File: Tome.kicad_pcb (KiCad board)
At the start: 2 copper layers, 13 x 1.4 mm, 155 parts, among them J201 USB_C_Receptacle_USB2.0_14P, J202 SD_Card_Receptacle, J203 [battery], J204 FFC Connector, J205 SM03B-SRSS-TB, J301 FFC Connector, J302 AudioJack3, J401 FPC Connector, J501 FPC Connector, J601 Conn_01x02_Pin, J602 Conn_01x02_Pin, J603 Conn_01x02_Pin, J604 Conn_01x02_Pin, J701 Conn_01x02_Pin, J702 Conn_01x02_Pin, J703 Conn_01x02_Pin, J704 Conn_01x02_Pin, Q201 DMG3415, Q202 DMG3415, Q401 Si1308EDL, Q501 Si1308EDL, SW201 [bootstrap button], SW202 [reset button], SW203 SW_SPST, SW301 SW_SPST, SW302 SW_SPST, SW601 RotaryEncoder_Switch, SW701 RotaryEncoder_Switch, U201 MCP73831-2-OT, U202 XC6220B331MR, U203 W25Q128JVS, U204 RP2350A, U205 74AHC1G04, U206 W25Q128JVS, U301 TLV70033_SOT23-5, U302 PCM5102A, U303 PAM8908, Y201 ABM8-272-T3

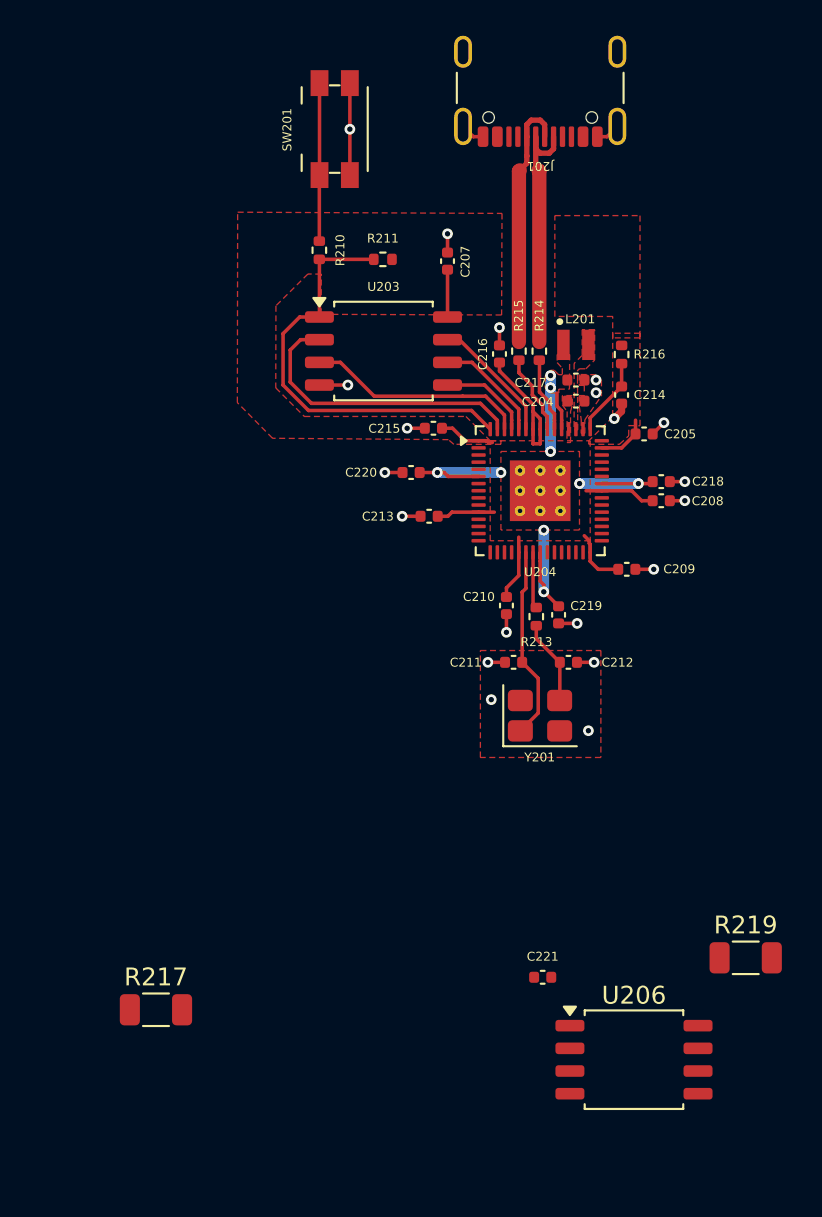
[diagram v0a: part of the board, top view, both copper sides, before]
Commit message: secondary flash
optional, don't anticipate needing it but who knows, could be useful
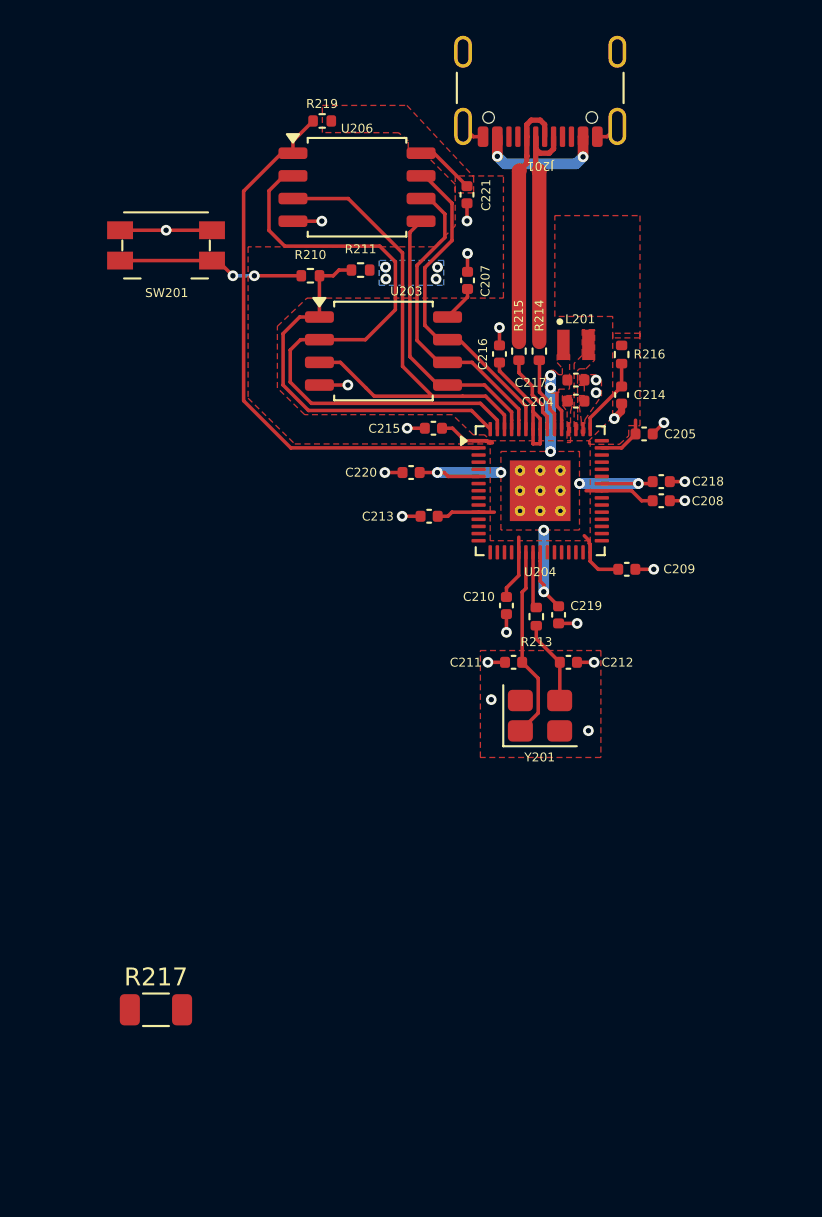
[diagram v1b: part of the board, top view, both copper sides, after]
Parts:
- R219: footprint Resistor_SMD:R_1206_3216Metric -> Resistor_SMD:R_0402_1005Metric
- moved R219 52.5 mm to (255.7, 22.9), turned to 180 degrees
- moved U206 51.3 mm to (257.6, 26.6)
- moved C221 44.0 mm to (263.8, 27.0), turned to 90 degrees
- moved SW201 11.5 mm to (247.0, 29.9), turned to 180 degrees
- moved C207 1.56 mm to (263.8, 31.8)
- moved R210 1.51 mm to (255.0, 31.6), turned to 0 degrees
- moved R211 1.39 mm to (257.9, 31.2)
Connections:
- J201 pad SH: GND -> (no net)
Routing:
- net FLASH_CS_2: track 0.00 -> 31.9 mm
- net QSPI_D1: track 16.7 -> 36.0 mm
- net QSPI_D2: track 12.4 -> 28.5 mm
- net QSPI_SCLK: track 6.19 -> 17.8 mm
- net QSPI_D3: track 7.22 -> 18.7 mm
- net QSPI_D0: track 5.17 -> 15.8 mm
- net +5V: track 0.00 -> 7.37 mm, vias 0 -> 2
- net +3V3: track 30.7 -> 33.4 mm, vias 0 -> 4
- net GND: track 23.1 -> 25.7 mm, vias 20 -> 22
- net FLASH_CS_1: track 24.2 -> 22.2 mm
- net Net-(R210-Pad1): track 8.85 -> 10.5 mm, vias 0 -> 2
- added copper zone on B.Cu, net +3V3

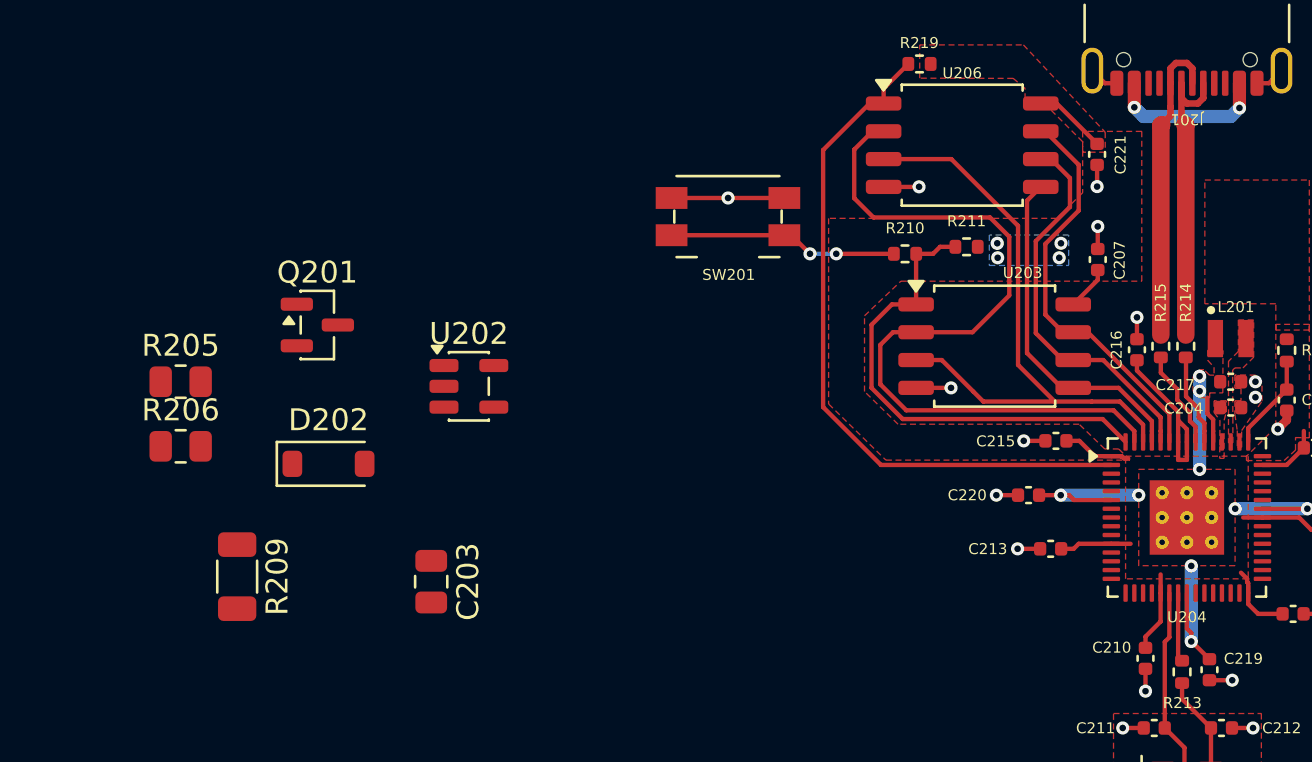
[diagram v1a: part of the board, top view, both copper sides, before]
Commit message: fixed ground fragmentation
don't break the ground plane under the qspi traces idiot
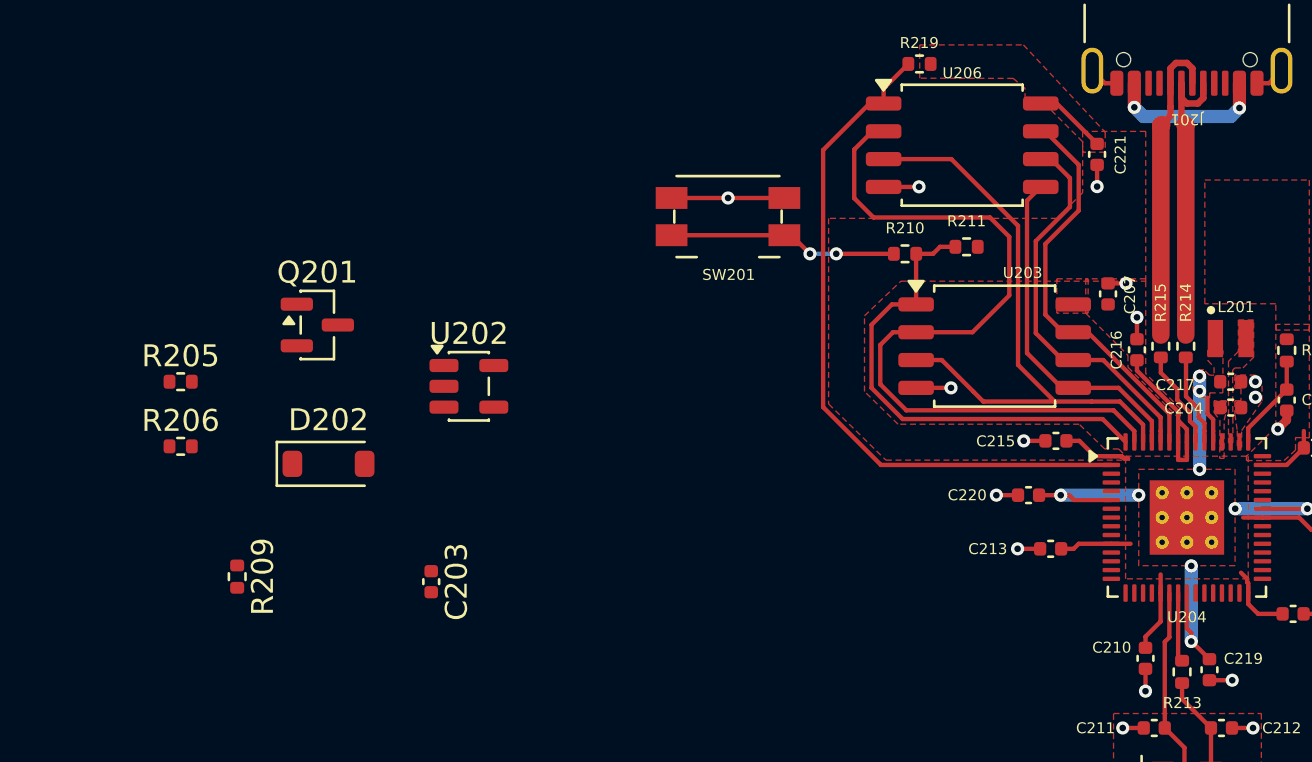
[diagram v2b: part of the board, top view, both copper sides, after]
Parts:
- C203: footprint Capacitor_SMD:C_0805_2012Metric -> Capacitor_SMD:C_0402_1005Metric
- R205, R206: footprint Resistor_SMD:R_0805_2012Metric -> Resistor_SMD:R_0402_1005Metric
- R209: footprint Resistor_SMD:R_1206_3216Metric -> Resistor_SMD:R_0402_1005Metric
- moved C207 1.64 mm to (264.3, 33.4)
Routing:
- net +3V3: track 33.4 -> 31.4 mm, vias 4 -> 0
- removed copper zone on B.Cu, net +3V3
